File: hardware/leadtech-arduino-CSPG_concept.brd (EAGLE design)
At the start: 100 x 80 mm, 46 parts, among them IC3 4050D, J1 CON_HEADER_1X08-PTH, J2 CON_HEADER_1X08-PTH, J3 CON_HEADER_1X08-PTH, J4 CON_HEADER_1X06-PTH, J5 CON_HEADER_1X05-PTH, J6 CON_HEADER_1X02-PTH, J9 CON_HEADER_1X02-PTH, P1 CON_HEADER_2X09, P2 CON_HEADER_2X09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

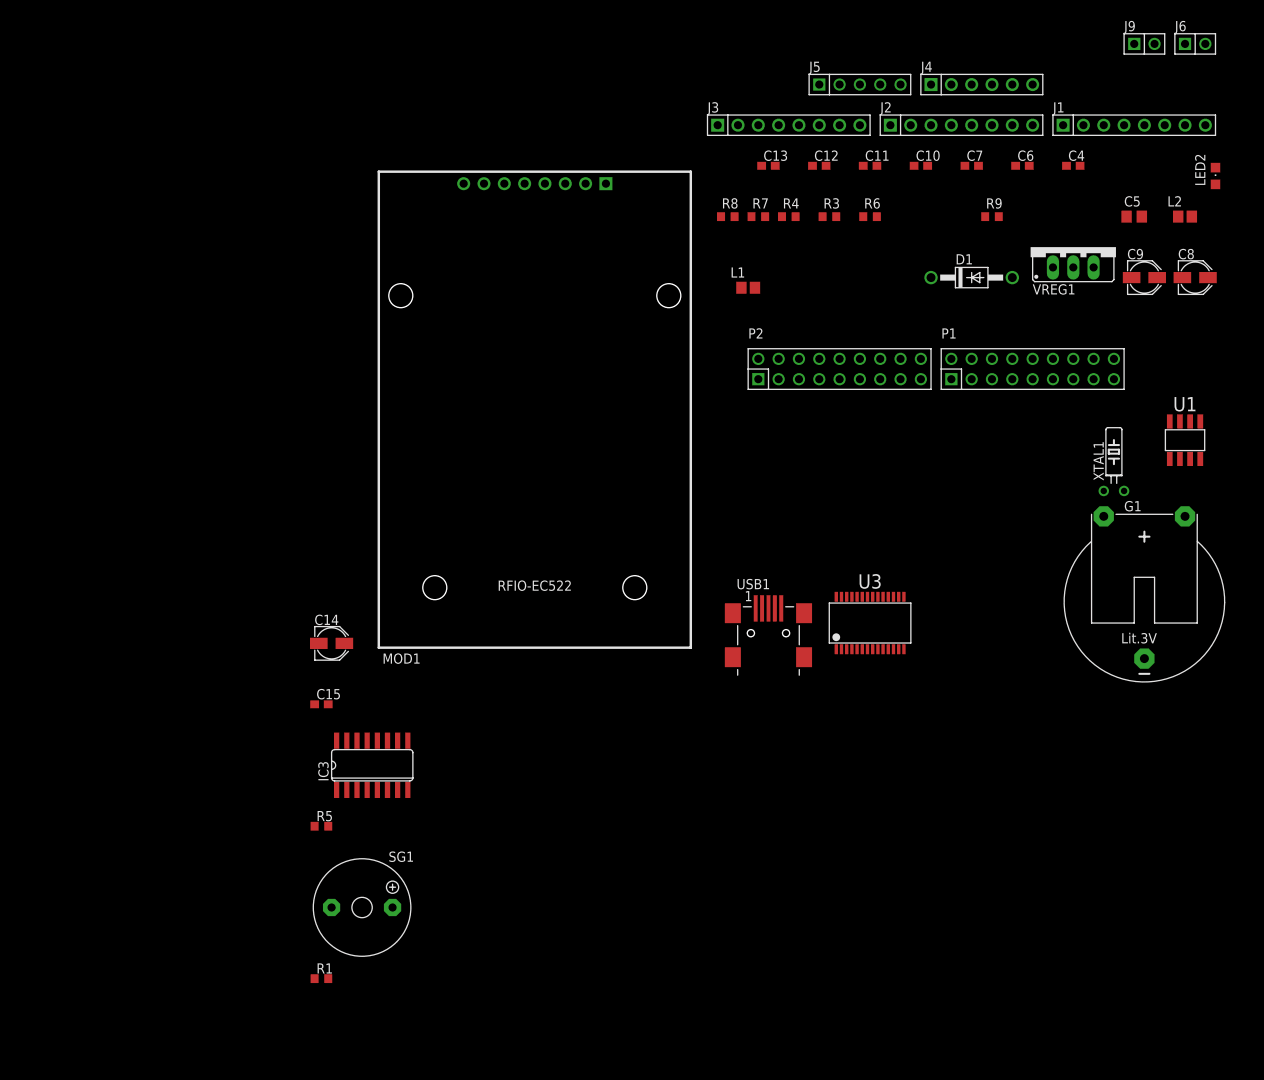
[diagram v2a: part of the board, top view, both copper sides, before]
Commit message: continue on schematic work, add i2c OLED
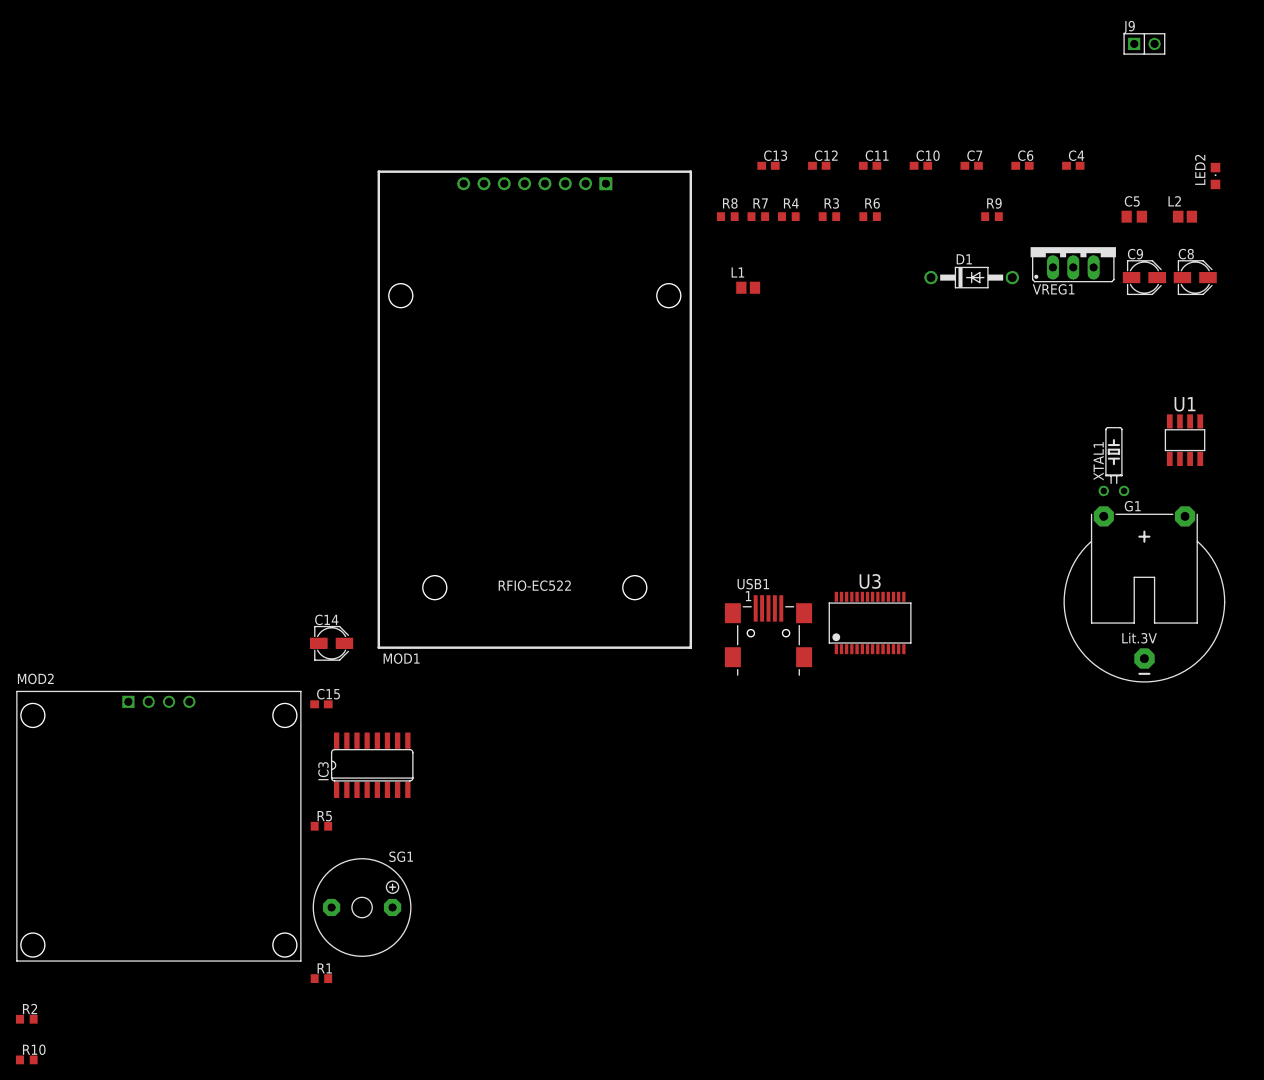
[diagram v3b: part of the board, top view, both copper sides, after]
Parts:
- removed J1, J2, J3: CON_HEADER_1X08-PTH, dp_devices.v6:M1X8
- removed J4: CON_HEADER_1X06-PTH, dp_devices.v6:M1X6
- removed J5: CON_HEADER_1X05-PTH, dp_devices.v6:M1X5
- removed J6: CON_HEADER_1X02-PTH, dp_devices.v6:M1X2
- removed P1, P2: CON_HEADER_2X09, dp_devices.v6:M2X9
- added MOD2: OLED_I2C_1.3, trosh_devices.eagle.v9:OLED_I2C_1.3
- added R10, R2: 10K, rcl:R0603
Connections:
- removed net ARDUINO-18: J5.5, P1.10
- removed net ARDUINO-20: J5.4, P1.8
- removed net ARDUINO-22: J5.3, P1.6
- removed net ARDUINO-24: J5.2, P1.4
- removed net ARDUINO-26: J5.1, P1.2
- new net DISPLAY_I2C_CLOCK: MOD2.P3, R2.1, U$1.25
- new net DISPLAY_I2C_DATA: MOD2.P4, R10.1, U$1.26
- net +5V: now also MOD2.P1, R10.2, R2.2; no longer J4.3, J6.1
- net GND: now also MOD2.P2; no longer J4.5, J6.2
- net PD7: no longer P1.14

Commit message: update files
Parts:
- removed R1: 10K, rcl:R0603
- moved USB1 139.9 mm to (52.1, 74.9), turned to 180 degrees
- moved R8 129.7 mm to (54.6, 52.1), turned to 270 degrees
- moved L1 128.4 mm to (54.6, 68.6), turned to 180 degrees
- moved U3 122.8 mm to (54.6, 58.4)
- moved R7 120.8 mm to (49.5, 52.1), turned to 270 degrees
- moved R4 119.6 mm to (52.1, 66.0), turned to 270 degrees
- moved R3 115.8 mm to (53.3, 66.0), turned to 270 degrees
- moved R6 108.2 mm to (50.8, 66.0), turned to 270 degrees
- moved C7 97.4 mm to (52.1, 52.1), turned to 270 degrees
- moved C4 90.2 mm to (58.4, 64.8), turned to 90 degrees
- moved C5 84.4 mm to (59.7, 68.6)
- moved C6 78.8 mm to (40.6, 63.5)
- moved L2 68.1 mm to (49.5, 68.6)
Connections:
- removed net N$1: R1.2, SG1.+
- net PIEZO: now also SG1.+; no longer R1.1

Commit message: 1
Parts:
- removed MOD1: RFIO-RC522, trosh_devices.eagle.v9:RFIO-RC522
- removed MOD2: OLED_I2C_1.3, trosh_devices.eagle.v9:OLED_I2C_1.3
- added J1: CON_HEADER_1X08-PTH, dp_devices.v6:M1X8
- added J2: CON_HEADER_1X04, dp_devices.v6:M1X4
- added J3: CON_HEADER_1X03-PTH, dp_devices.v6:M1X3
- moved R5 228.9 mm to (95.2, 41.9)
- moved C15 216.2 mm to (81.3, 59.7)
- moved IC3 215.1 mm to (81.3, 67.3), turned to 90 degrees
- moved R10 175.3 mm to (1.27, 15.2)
- moved R2 175.3 mm to (1.27, 20.3)
- moved SG1 171.6 mm to (34.3, 45.7)
- moved C10 138.6 mm to (81.3, 22.9)
- moved C14 133.3 mm to (7.62, 22.9)
- moved C12 122.6 mm to (57.1, 43.2), turned to 180 degrees
- moved C13 120.1 mm to (48.3, 43.2)
- moved XTAL1 117.3 mm to (90.2, 16.5)
- moved C11 115.8 mm to (50.8, 22.9)
- moved U1 103.8 mm to (85.1, 16.5)
- moved G1 95.3 mm to (72.4, 11.4)
- moved R9 60.4 mm to (16.5, 73.7)
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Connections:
- new net N$1: J3.3
- new net N$2: J3.2
- net +3V3: now also J1.8; no longer MOD1.P8
- net +5V: now also J2.1, LED2.A; no longer MOD2.P1
- net DISPLAY_I2C_CLOCK: now also J2.3; no longer MOD2.P3
- net DISPLAY_I2C_DATA: now also J2.4; no longer MOD2.P4
- net GND: now also J1.6, J2.2, J3.1; no longer MOD1.P6, MOD2.P2
- net RFID_CLOCK_3V: now also J1.2; no longer MOD1.P2
- net RFID_DATA_3V: now also J1.1; no longer MOD1.P1
- net RFID_MISO: now also J1.4; no longer MOD1.P4
- net RFID_MOSI_3V: now also J1.3; no longer MOD1.P3
- net RFID_RESET_3V: now also J1.7; no longer MOD1.P7

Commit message: edit CSPG arduino hardware
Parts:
- added R1: 10K, rcl:R0603
- added U$2: (no value), trosh_devices.eagle.v9:GIZDUINOX
- moved USB1 48.4 mm to (5.08, 63.5), turned to 270 degrees
- moved C5 48.3 mm to (11.4, 71.1), turned to 90 degrees
- moved C4 43.5 mm to (15.2, 69.8), turned to 180 degrees
- moved L1 43.3 mm to (11.4, 66.0), turned to 270 degrees
- moved C8 41.5 mm to (43.2, 49.5)
- moved D1 41.5 mm to (49.5, 54.6)
- moved J9 41.5 mm to (44.5, 59.7)
- moved LED2 41.5 mm to (54.6, 59.7)
- moved R9 41.5 mm to (54.6, 57.1)
- moved R3 39.4 mm to (14.0, 64.8), turned to 0 degrees
- moved L2 38.9 mm to (11.4, 61.0), turned to 90 degrees
- moved R4 38.2 mm to (14.0, 63.5), turned to 0 degrees
- moved R6 37.0 mm to (14.0, 62.2), turned to 0 degrees
- moved U3 33.9 mm to (21.6, 66.0), turned to 90 degrees
- moved SG1 32.1 mm to (7.62, 27.9)
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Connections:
- new net N$3: R1.1, U$1.20
- net +5V: now also R1.2
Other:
- board size 100 x 80 mm -> 53.3 x 80 mm

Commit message: worked on schematic
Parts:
- added IC1: OP-AMP, SparkFun-IC-Amplifiers:SO08
- added Q2: (no value), dp_devices.v6:SOT-23
- added R11: 330R, dp_devices.v6:R603
- added VREG2: 3.3V, dp_devices.v6:SOT-223
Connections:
- new net N$4: IC1.1, Q2.1
- net +3V3: now also IC1.2, VREG2.2
- net +5V: now also IC1.8, Q2.2, VREG2.3
- net GND: now also IC1.4, VREG2.1
- net VUSB: now also Q2.3

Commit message: 1
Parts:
- added C1: 10uF, dp_devices.v6:CASE_B
- added R12: 10K, dp_devices.v6:R603
- R11: value 330R -> 10K
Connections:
- removed net N$20: C8.+, D1.C, VREG1.3
- new net N$5: IC1.3, R11.1, R12.2
- new net VIN: C8.+, D1.C, R11.2, VREG1.3
- net +3V3: now also C1.+
- net GND: now also C1.-, R12.1
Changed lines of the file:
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@@
 <?xml version="1.0" encoding="utf-8"?>
 <!DOCTYPE eagle SYSTEM "eagle.dtd">
-<eagle version="9.1.3">
+<eagle version="9.4.2">
 <drawing>
 <settings>
@@
 <attribute name="VALUE" x="0.635" y="13.335" size="1.27" layer="27"/>
 </element>
-<element name="J1" library="dp_devices.v6" package="M1X8" value="CON_HEADER_1X08-PTH" x="81.28" y="76.2" rot="R180"/>
-<element name="J2" library="dp_devices.v6" package="M1X4" value="CON_HEADER_1X04" x="41.91" y="67.31"/>
-<element name="J3" library="dp_devices.v6" package="M1X3" value="CON_HEADER_1X03-PTH" x="2.54" y="8.89"/>
-<element name="U$2" library="trosh_devices.eagle.v9" package="GIZDUINOX" value="" x="0" y="0" locked="yes"/>
-<element name="R1" library="rcl" library_urn="urn:adsk.eagle:library:334" package="R0603" package3d_urn="urn:adsk.eagle:package:23555/3" value="10K" x="1.27" y="-3.81">
+<element name="J1" library="dp_devices.v6" package="M1X8" value="CON_HEADER_1X08-PTH" x="81.28" y="76.2" smashed="yes" rot="R180">
+<attribute name="NAME" x="91.44" y="74.6125" size="1.27" layer="25" ratio="10" rot="R180"/>
+</element>
+<element name="J2" library="dp_devices.v6" package="M1X4" value="CON_HEADER_1X04" x="41.91" y="67.31" smashed="yes">
+<attribute name="NAME" x="40.64" y="68.8975" size="1.27" layer="25" ratio="10"/>
+</element>
+<element name="J3" library="dp_devices.v6" package="M1X3" value="CON_HEADER_1X03-PTH" x="2.54" y="8.89" smashed="yes">
+<attribute name="NAME" x="1.27" y="10.4775" size="1.27" layer="25" ratio="10"/>
+</element>
+<element name="U$2" library="trosh_devices.eagle.v9" package="GIZDUINOX" value="" x="0" y="0" locked="yes" smashed="yes">
+<attribute name="NAME" x="0" y="82.55" size="1.27" layer="25"/>
+<attribute name="VALUE" x="0" y="81.28" size="1.27" layer="27"/>
+</element>
+<element name="R1" library="rcl" library_urn="urn:adsk.eagle:library:334" package="R0603" package3d_urn="urn:adsk.eagle:package:23555/3" value="10K" x="1.27" y="-3.81" smashed="yes">
+<attribute name="NAME" x="0.635" y="-3.175" size="1.27" layer="25"/>
 <attribute name="SPICEPREFIX" value="R" x="1.27" y="-3.81" size="1.778" layer="27" display="off"/>
-</element>
-<element name="IC1" library="SparkFun-IC-Amplifiers" package="SO08" value="OP-AMP" x="3.81" y="-10.16">
+<attribute name="VALUE" x="0.635" y="-5.715" size="1.27" layer="27"/>
+</element>
+<element name="IC1" library="SparkFun-IC-Amplifiers" package="SO08" value="OP-AMP" x="3.81" y="-10.16" smashed="yes">
+<attribute name="NAME" x="0.635" y="-10.16" size="0.6096" layer="25" font="vector" ratio="20" rot="R90" align="bottom-center"/>
 <attribute name="PROD_ID" value="NA-XXXXX" x="3.81" y="-10.16" size="1.778" layer="27" display="off"/>
-</element>
-<element name="Q2" library="dp_devices.v6" package="SOT-23" value="" x="-6.35" y="-8.89"/>
-<element name="R11" library="dp_devices.v6" package="R603" value="330R" x="-6.35" y="-16.51"/>
-<element name="VREG2" library="dp_devices.v6" package="SOT-223" value="3.3V" x="-12.7" y="-12.7"/>
+<attribute name="VALUE" x="7.62" y="-10.16" size="0.6096" layer="27" font="vector" ratio="20" rot="R90" align="bottom-center"/>
+</element>
+<element name="Q2" library="dp_devices.v6" package="SOT-23" value="" x="-6.35" y="-8.89" smashed="yes">
+<attribute name="NAME" x="-8.255" y="-6.6675" size="1.27" layer="25" font="vector" ratio="10"/>
+<attribute name="VALUE" x="-8.255" y="-12.3825" size="1.27" layer="27" font="vector" ratio="10"/>
+</element>
+<element name="R11" library="dp_devices.v6" package="R603" value="10K" x="-6.35" y="-16.51" smashed="yes">
+<attribute name="NAME" x="-7.112" y="-15.494" size="1.27" layer="25" font="vector" ratio="10"/>
+<attribute name="VALUE" x="-7.112" y="-18.796" size="1.27" layer="27" font="vector" ratio="10"/>
+</element>
+<element name="VREG2" library="dp_devices.v6" package="SOT-223" value="3.3V" x="-12.7" y="-12.7" smashed="yes">
+<attribute name="NAME" x="-16.1925" y="-7.9375" size="1.27" layer="25" font="vector" ratio="10"/>
+<attribute name="VALUE" x="-15.875" y="-18.7325" size="1.27" layer="27" font="vector" ratio="10"/>
+</element>
+<element name="C1" library="dp_devices.v6" package="CASE_B" value="10uF" x="-22.86" y="-13.97" smashed="yes">
+<attribute name="NAME" x="-25.01" y="-11.67" size="1.27" layer="25" ratio="10"/>
+<attribute name="VALUE" x="-25.01" y="-17.5625" size="1.27" layer="27" ratio="10"/>
+</element>
+<element name="R12" library="dp_devices.v6" package="R603" value="10K" x="-24.13" y="-22.86" smashed="yes">
+<attribute name="NAME" x="-24.892" y="-21.844" size="1.27" layer="25" font="vector" ratio="10"/>
+<attribute name="VALUE" x="-24.892" y="-25.146" size="1.27" layer="27" font="vector" ratio="10"/>
+</element>
 </elements>
 <signals>
@@
 <contactref element="VREG2" pad="1"/>
 <contactref element="IC1" pad="4"/>
+<contactref element="C1" pad="-"/>
+<contactref element="R12" pad="1"/>
 <wire x1="77.47" y1="76.2" x2="84.3534" y2="71.755" width="0" layer="19" extent="1-1"/>
 <wire x1="80.43" y1="59.69" x2="84.3534" y2="71.755" width="0" layer="19" extent="1-1"/>
@@
 <wire x1="5.715" y1="-12.96" x2="2.54" y2="8.89" width="0" layer="19" extent="1-1"/>
 <wire x1="-15" y1="-15.85" x2="5.715" y2="-12.96" width="0" layer="19" extent="1-1"/>
+<wire x1="-24.46" y1="-13.97" x2="-15" y2="-15.85" width="0" layer="19" extent="1-1"/>
+<wire x1="-24.98" y1="-22.86" x2="-24.46" y2="-13.97" width="0" layer="19" extent="1-1"/>
 <wire x1="82.13" y1="22.86" x2="80.43" y2="59.69" width="0" layer="19" extent="1-1"/>
 <wire x1="86.995" y1="14.17" x2="82.13" y2="22.86" width="0" layer="19" extent="1-1"/>
@@
 <wire x1="45.72" y1="59.69" x2="49.53" y2="59.69" width="0" layer="19" extent="1-1"/>
 </signal>
-<signal name="N$20">
-<contactref element="D1" pad="C"/>
-<contactref element="C8" pad="+"/>
-<contactref element="VREG1" pad="3"/>
-<wire x1="44.78" y1="49.53" x2="49.53" y2="49.53" width="0" layer="19" extent="1-1"/>
-<wire x1="5.08" y1="40.64" x2="44.78" y2="49.53" width="0" layer="19" extent="1-1"/>
-</signal>
 <signal name="N$21">
 <contactref element="LED2" pad="C"/>
@@
 <contactref element="VREG2" pad="2"/>
 <contactref element="IC1" pad="2"/>
+<contactref element="C1" pad="+"/>
 <wire x1="84.3534" y1="62.865" x2="72.39" y2="76.2" width="0" layer="19" extent="1-1"/>
 <wire x1="82.13" y1="59.69" x2="84.3534" y2="62.865" width="0" layer="19" extent="1-1"/>
@@
 <wire x1="3.175" y1="-12.96" x2="9.22" y2="22.86" width="0" layer="19" extent="1-1"/>
 <wire x1="-12.7" y1="-15.85" x2="3.175" y2="-12.96" width="0" layer="19" extent="1-1"/>
+<wire x1="-21.26" y1="-13.97" x2="-12.7" y2="-15.85" width="0" layer="19" extent="1-1"/>
 </signal>
 <signal name="RFID_DATA_3V">
@@
 <wire x1="-7.3" y1="-9.99" x2="1.905" y2="-12.96" width="0" layer="19" extent="1-1"/>
 </signal>
+<signal name="N$5">
+<contactref element="IC1" pad="3"/>
+<contactref element="R11" pad="1"/>
+<contactref element="R12" pad="2"/>
+<wire x1="-7.2" y1="-16.51" x2="-23.28" y2="-22.86" width="0" layer="19" extent="1-1"/>
+<wire x1="4.445" y1="-12.96" x2="-7.2" y2="-16.51" width="0" layer="19" extent="1-1"/>
+</signal>
+<signal name="VIN">
+<contactref element="D1" pad="C"/>
+<contactref element="C8" pad="+"/>
+<contactref element="VREG1" pad="3"/>
+<contactref element="R11" pad="2"/>
+<wire x1="44.78" y1="49.53" x2="49.53" y2="49.53" width="0" layer="19" extent="1-1"/>
+<wire x1="5.08" y1="40.64" x2="44.78" y2="49.53" width="0" layer="19" extent="1-1"/>
+<wire x1="-5.5" y1="-16.51" x2="5.08" y2="40.64" width="0" layer="19" extent="1-1"/>
+</signal>
 </signals>
